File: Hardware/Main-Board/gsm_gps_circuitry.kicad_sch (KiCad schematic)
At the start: 51 parts, among them J10 SIM8060-6-1-14-00-A, J4 UFL, J5 UFL, J6 UFL, Q1 3416, Q2 3416, Q3 MMBT2222A, Q4 MMBT2222A, U1 SIM7600G, U11 TPS22810DRV

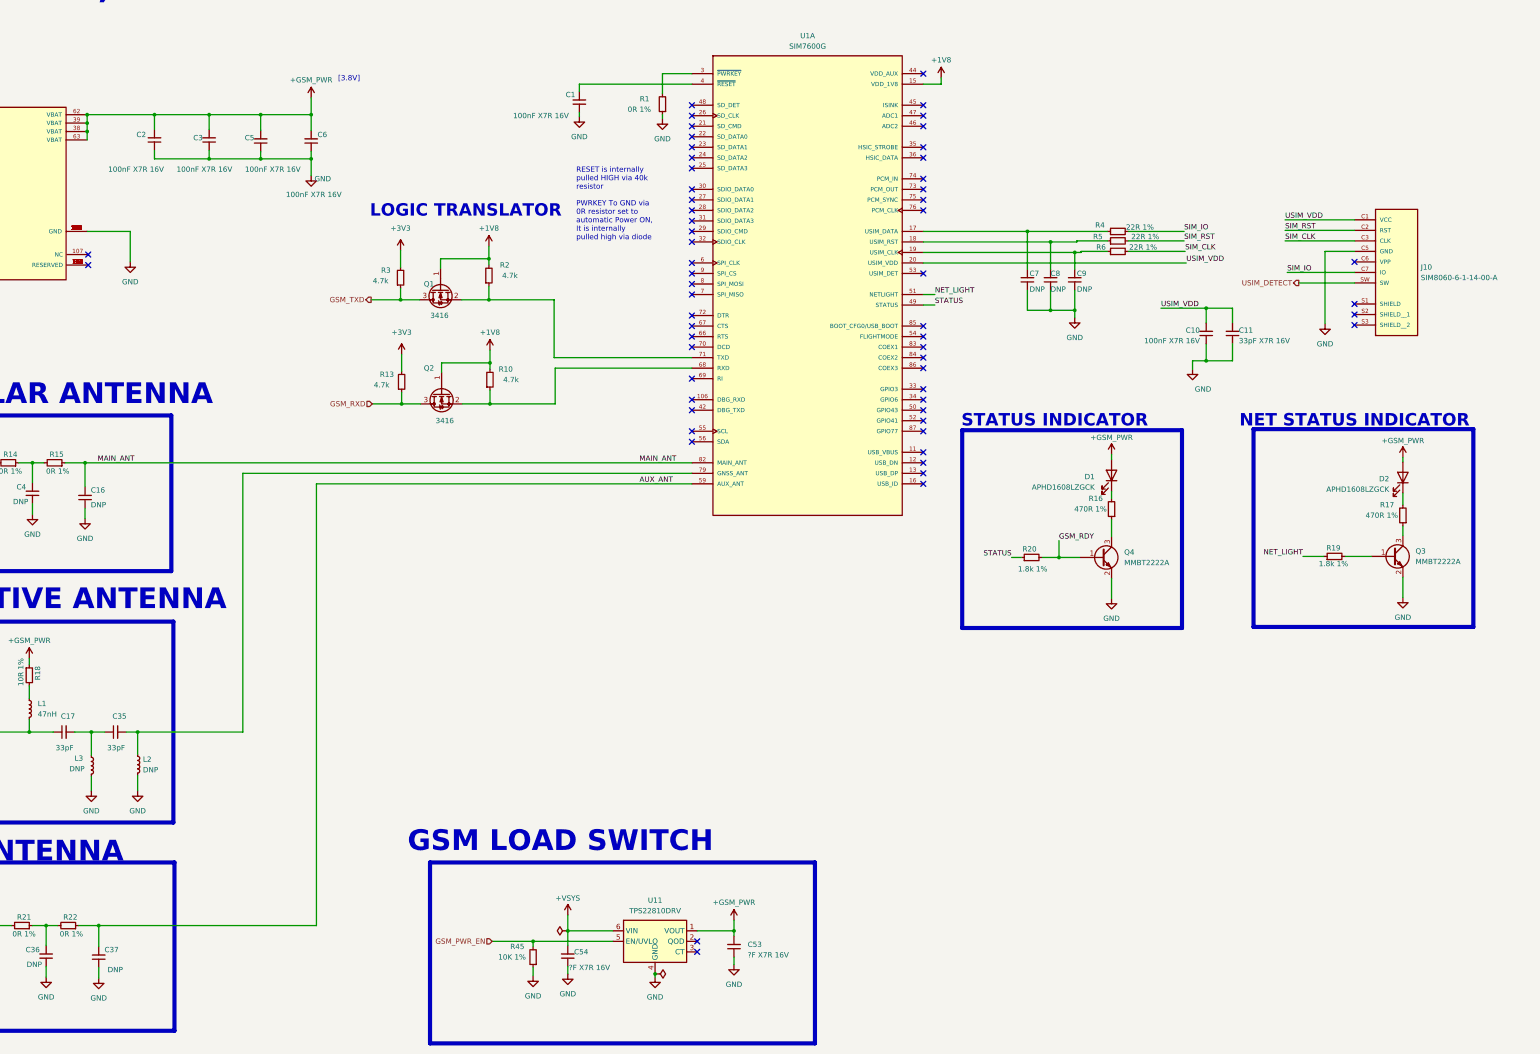
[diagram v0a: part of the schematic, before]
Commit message: Done with main board design, and camera interconnect in progress
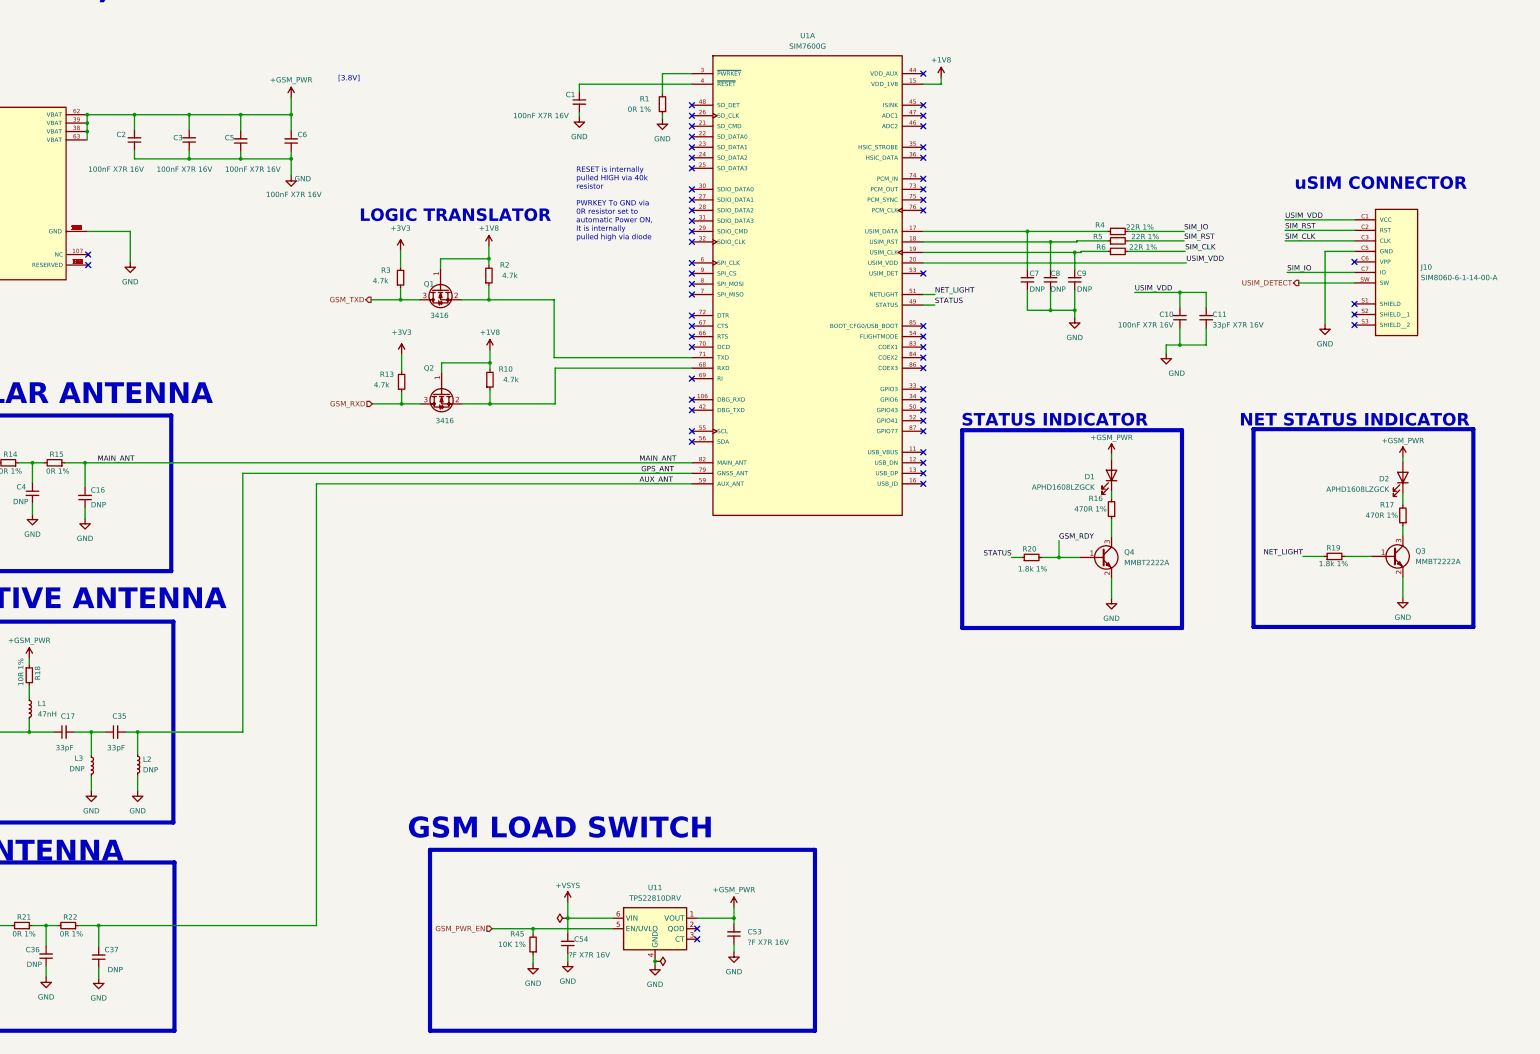
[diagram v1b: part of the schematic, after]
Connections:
- net GPS_ANT: now reaches C35.2, L2.1, U1.79 (GNSS_ANT)
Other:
- note added: "uSIM CONNECTOR"
- moved on the sheet: C10, C11, C2, C3, C5, C53, C54, C6, R45, U11
